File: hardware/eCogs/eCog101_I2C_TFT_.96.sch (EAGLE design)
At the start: 2 parts

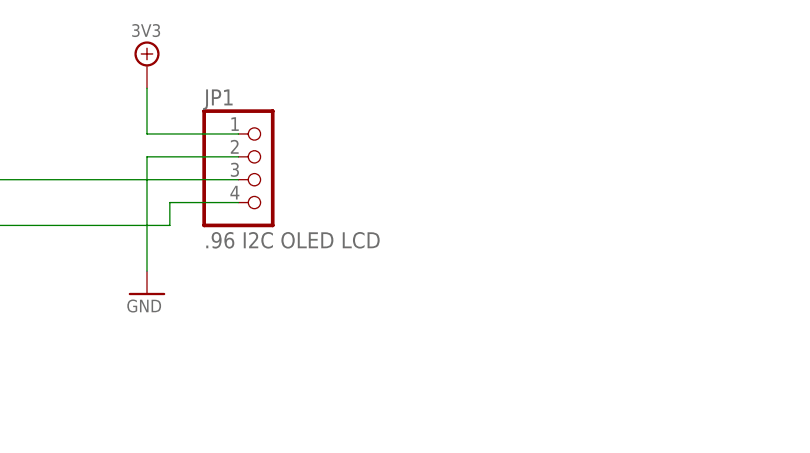
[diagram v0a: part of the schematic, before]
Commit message: Put connector for both types of power schemes.
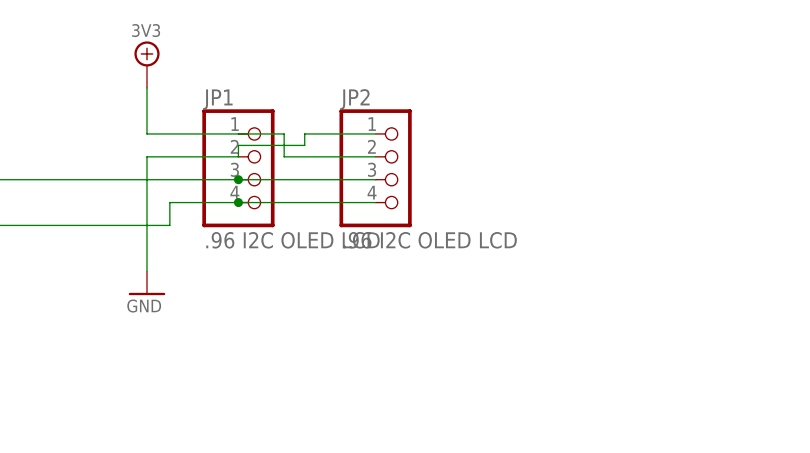
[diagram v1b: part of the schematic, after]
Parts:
- added JP2: .96 I2C OLED LCD, pinhead:PINHD-1X4
- ECOG: value ECOG_BUSES_ROWSURFACEMOUNT -> ECOG_BUSES_ROWTHROUGHHOLE; device eCogs:ECOG_BUSES_ROWSURFACEMOUNT -> eCogs:ECOG_BUSES_ROWTHROUGHHOLE
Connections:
- net 3V3: now also JP2.2
- net GND: now also JP2.1
- net N$1: now also JP2.3
- net N$2: now also JP2.4
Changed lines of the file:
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@@
 <grid distance="0.1" unitdist="inch" unit="inch" style="lines" multiple="1" display="no" altdistance="0.01" altunitdist="inch" altunit="inch"/>
 <layers>
-<layer number="1" name="Top" color="4" fill="1" visible="no" active="no"/>
-<layer number="2" name="Route2" color="1" fill="3" visible="no" active="no"/>
-<layer number="3" name="Route3" color="4" fill="3" visible="no" active="no"/>
-<layer number="4" name="Route4" color="1" fill="4" visible="no" active="no"/>
-<layer number="13" name="Route13" color="4" fill="5" visible="no" active="no"/>
-<layer number="14" name="Route14" color="1" fill="6" visible="no" active="no"/>
-<layer number="15" name="Route15" color="4" fill="6" visible="no" active="no"/>
-<layer number="16" name="Bottom" color="1" fill="1" visible="no" active="no"/>
-<layer number="17" name="Pads" color="2" fill="1" visible="no" active="no"/>
-<layer number="18" name="Vias" color="2" fill="1" visible="no" active="no"/>
-<layer number="19" name="Unrouted" color="6" fill="1" visible="no" active="no"/>
-<layer number="20" name="Dimension" color="15" fill="1" visible="no" active="no"/>
-<layer number="21" name="tPlace" color="16" fill="1" visible="no" active="no"/>
-<layer number="22" name="bPlace" color="14" fill="1" visible="no" active="no"/>
-<layer number="23" name="tOrigins" color="15" fill="1" visible="no" active="no"/>
-<layer number="24" name="bOrigins" color="15" fill="1" visible="no" active="no"/>
-<layer number="25" name="tNames" color="16" fill="1" visible="no" active="no"/>
-<layer number="26" name="bNames" color="7" fill="1" visible="no" active="no"/>
-<layer number="27" name="tValues" color="7" fill="1" visible="no" active="no"/>
-<layer number="28" name="bValues" color="7" fill="1" visible="no" active="no"/>
+<layer number="1" name="Top" color="4" fill="1" visible="yes" active="no"/>
+<layer number="2" name="Route2" color="1" fill="3" visible="yes" active="no"/>
+<layer number="3" name="Route3" color="4" fill="3" visible="yes" active="no"/>
+<layer number="4" name="Route4" color="1" fill="4" visible="yes" active="no"/>
+<layer number="13" name="Route13" color="4" fill="5" visible="yes" active="no"/>
+<layer number="14" name="Route14" color="1" fill="6" visible="yes" active="no"/>
+<layer number="15" name="Route15" color="4" fill="6" visible="yes" active="no"/>
+<layer number="16" name="Bottom" color="1" fill="1" visible="yes" active="no"/>
+<layer number="17" name="Pads" color="2" fill="1" visible="yes" active="no"/>
+<layer number="18" name="Vias" color="2" fill="1" visible="yes" active="no"/>
+<layer number="19" name="Unrouted" color="6" fill="1" visible="yes" active="no"/>
+<layer number="20" name="Dimension" color="15" fill="1" visible="yes" active="no"/>
+<layer number="21" name="tPlace" color="16" fill="1" visible="yes" active="no"/>
+<layer number="22" name="bPlace" color="14" fill="1" visible="yes" active="no"/>
+<layer number="23" name="tOrigins" color="15" fill="1" visible="yes" active="no"/>
+<layer number="24" name="bOrigins" color="15" fill="1" visible="yes" active="no"/>
+<layer number="25" name="tNames" color="16" fill="1" visible="yes" active="no"/>
+<layer number="26" name="bNames" color="7" fill="1" visible="yes" active="no"/>
+<layer number="27" name="tValues" color="7" fill="1" visible="yes" active="no"/>
+<layer number="28" name="bValues" color="7" fill="1" visible="yes" active="no"/>
 <layer number="29" name="tStop" color="7" fill="3" visible="no" active="no"/>
 <layer number="30" name="bStop" color="7" fill="6" visible="no" active="no"/>
@@
 <layer number="35" name="tGlue" color="7" fill="4" visible="no" active="no"/>
 <layer number="36" name="bGlue" color="7" fill="5" visible="no" active="no"/>
-<layer number="37" name="tTest" color="7" fill="1" visible="no" active="no"/>
-<layer number="38" name="bTest" color="7" fill="1" visible="no" active="no"/>
+<layer number="37" name="tTest" color="7" fill="1" visible="yes" active="no"/>
+<layer number="38" name="bTest" color="7" fill="1" visible="yes" active="no"/>
 <layer number="39" name="tKeepout" color="4" fill="11" visible="no" active="no"/>
 <layer number="40" name="bKeepout" color="1" fill="11" visible="no" active="no"/>
@@
 <layer number="44" name="Drills" color="7" fill="1" visible="no" active="no"/>
 <layer number="45" name="Holes" color="7" fill="1" visible="no" active="no"/>
-<layer number="46" name="Milling" color="3" fill="1" visible="no" active="no"/>
-<layer number="47" name="Measures" color="7" fill="1" visible="no" active="no"/>
-<layer number="48" name="Document" color="7" fill="1" visible="no" active="no"/>
-<layer number="49" name="Reference" color="7" fill="1" visible="no" active="no"/>
-<layer number="50" name="dxf" color="7" fill="1" visible="no" active="no"/>
-<layer number="51" name="tDocu" color="6" fill="1" visible="no" active="no"/>
-<layer number="52" name="bDocu" color="7" fill="1" visible="no" active="no"/>
-<layer number="53" name="tGND_GNDA" color="7" fill="9" visible="no" active="no"/>
-<layer number="54" name="bGND_GNDA" color="1" fill="9" visible="no" active="no"/>
-<layer number="56" name="wert" color="3" fill="1" visible="no" active="no"/>
-<layer number="57" name="tCAD" color="7" fill="1" visible="no" active="no"/>
-<layer number="59" name="tCarbon" color="7" fill="1" visible="no" active="no"/>
-<layer number="60" name="bCarbon" color="7" fill="1" visible="no" active="no"/>
+<layer number="46" name="Milling" color="3" fill="1" visible="yes" active="no"/>
+<layer number="47" name="Measures" color="7" fill="1" visible="yes" active="no"/>
+<layer number="48" name="Document" color="7" fill="1" visible="yes" active="no"/>
+<layer number="49" name="Reference" color="7" fill="1" visible="yes" active="no"/>
+<layer number="50" name="dxf" color="7" fill="1" visible="yes" active="no"/>
+<layer number="51" name="tDocu" color="6" fill="1" visible="yes" active="no"/>
+<layer number="52" name="bDocu" color="7" fill="1" visible="yes" active="no"/>
+<layer number="53" name="tGND_GNDA" color="7" fill="9" visible="yes" active="no"/>
+<layer number="54" name="bGND_GNDA" color="1" fill="9" visible="yes" active="no"/>
+<layer number="56" name="wert" color="3" fill="1" visible="yes" active="no"/>
+<layer number="57" name="tCAD" color="7" fill="1" visible="yes" active="no"/>
+<layer number="59" name="tCarbon" color="7" fill="1" visible="yes" active="no"/>
+<layer number="60" name="bCarbon" color="7" fill="1" visible="yes" active="no"/>
 <layer number="90" name="Modules" color="7" fill="1" visible="yes" active="yes"/>
 <layer number="91" name="Nets" color="2" fill="1" visible="yes" active="yes"/>
@@
 <part name="FRAME1" library="frames" deviceset="A3L-LOC" device=""/>
 <part name="GND2" library="GadgetFactory" deviceset="GND" device=""/>
-<part name="ECOG" library="eCogs" deviceset="ECOG_BUSES_ROW" device="SURFACEMOUNT" value="ECOG_BUSES_ROWSURFACEMOUNT"/>
+<part name="ECOG" library="eCogs" deviceset="ECOG_BUSES_ROW" device="THROUGHHOLE" value="ECOG_BUSES_ROWTHROUGHHOLE"/>
 <part name="JP1" library="pinhead" deviceset="PINHD-1X4" device="" value=".96 I2C OLED LCD">
 <attribute name="DEALEXTREME" value="419232"/>
@@
 <part name="GND1" library="GadgetFactory" deviceset="GND" device=""/>
 <part name="3V3_PWR2" library="GadgetFactory" deviceset="3V3" device=""/>
+<part name="JP2" library="pinhead" deviceset="PINHD-1X4" device="" value=".96 I2C OLED LCD">
+<attribute name="DEALEXTREME" value="419232"/>
+</part>
 </parts>
 <sheets>
@@
 <instance part="GND1" gate="A" x="93.98" y="60.96"/>
 <instance part="3V3_PWR2" gate="A" x="93.98" y="86.36"/>
+<instance part="JP2" gate="A" x="121.92" y="73.66">
+<attribute name="DEALEXTREME" x="121.92" y="73.66" size="1.778" layer="96" display="off"/>
+</instance>
 </instances>
 <busses>
@@
 <wire x1="104.14" y1="76.2" x2="93.98" y2="76.2" width="0.2032" layer="91"/>
 <wire x1="93.98" y1="76.2" x2="93.98" y2="63.5" width="0.2032" layer="91"/>
+<pinref part="JP2" gate="A" pin="1"/>
+<wire x1="119.38" y1="78.74" x2="111.506" y2="78.74" width="0.2032" layer="91"/>
+<wire x1="111.506" y1="78.74" x2="111.506" y2="77.47" width="0.2032" layer="91"/>
+<wire x1="111.506" y1="77.47" x2="104.14" y2="77.47" width="0.2032" layer="91"/>
+<wire x1="104.14" y1="77.47" x2="104.14" y2="76.2" width="0.2032" layer="91"/>
 </segment>
 </net>
@@
 <wire x1="104.14" y1="78.74" x2="93.98" y2="78.74" width="0.2032" layer="91"/>
 <wire x1="93.98" y1="78.74" x2="93.98" y2="83.82" width="0.2032" layer="91"/>
+<wire x1="104.14" y1="78.74" x2="109.22" y2="78.74" width="0.2032" layer="91"/>
+<wire x1="109.22" y1="78.74" x2="109.22" y2="76.2" width="0.2032" layer="91"/>
+<pinref part="JP2" gate="A" pin="2"/>
+<wire x1="109.22" y1="76.2" x2="119.38" y2="76.2" width="0.2032" layer="91"/>
 </segment>
 <segment>
@@
 <pinref part="JP1" gate="A" pin="4"/>
 <wire x1="96.52" y1="71.12" x2="104.14" y2="71.12" width="0.2032" layer="91"/>
+<pinref part="JP2" gate="A" pin="4"/>
+<junction x="104.14" y="71.12"/>
+<wire x1="104.14" y1="71.12" x2="119.38" y2="71.12" width="0.1524" layer="91"/>
 </segment>
 </net>
@@
 <pinref part="ECOG" gate="ECOG_BUSES" pin="I2C-SCL@B5"/>
 <wire x1="71.12" y1="71.12" x2="63.5" y2="71.12" width="0.2032" layer="91"/>
-</segment>
-</net>
+<pinref part="JP2" gate="A" pin="3"/>
+<junction x="104.14" y="73.66"/>
+<wire x1="104.14" y1="73.66" x2="119.38" y2="73.66" width="0.1524" layer="91"/>
+</segment>
+</net>
